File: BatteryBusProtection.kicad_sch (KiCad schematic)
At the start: 14 parts, among them Q10 SIRA99DP-T1-GE3, Q7 SIRA99DP-T1-GE3, Q8 SIRA99DP-T1-GE3, Q9 SIRA99DP-T1-GE3, U3 LTC4412xS6, U4 LTC4412xS6

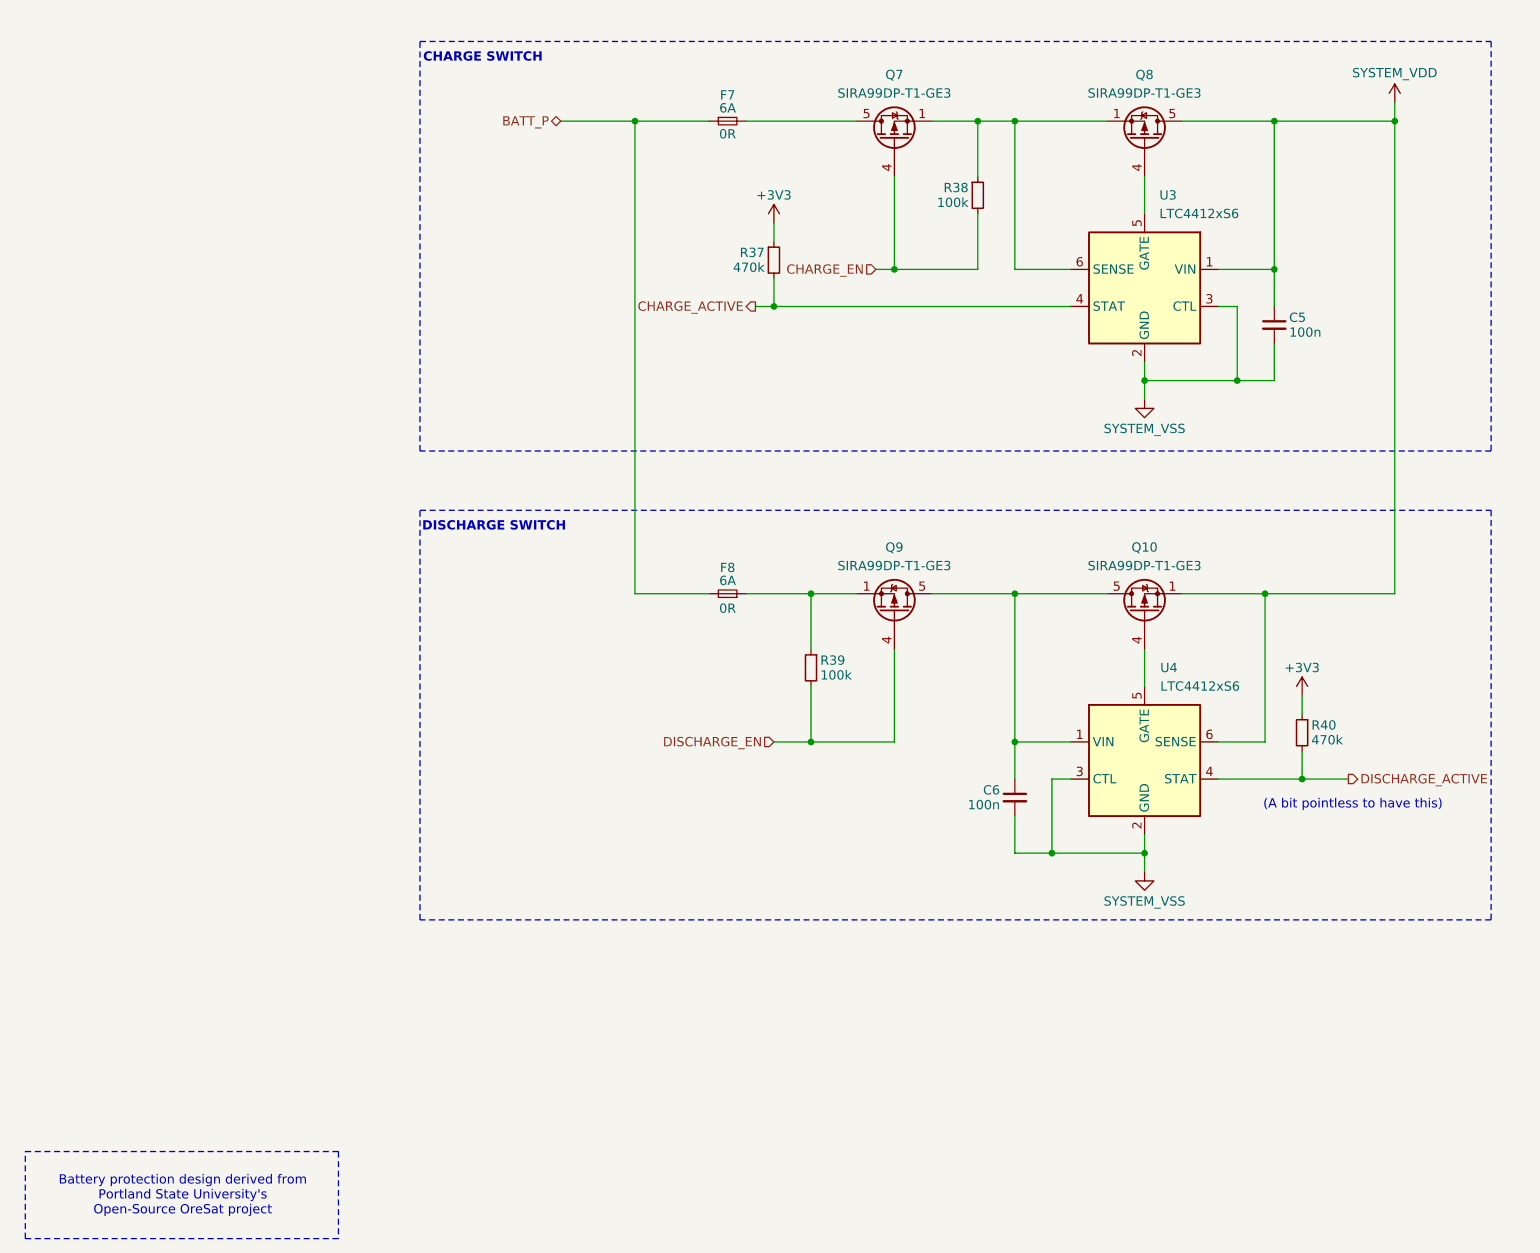
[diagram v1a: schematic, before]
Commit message: v3.2 Updates
Added 0ohm bypass. Opto-isolated heater enables
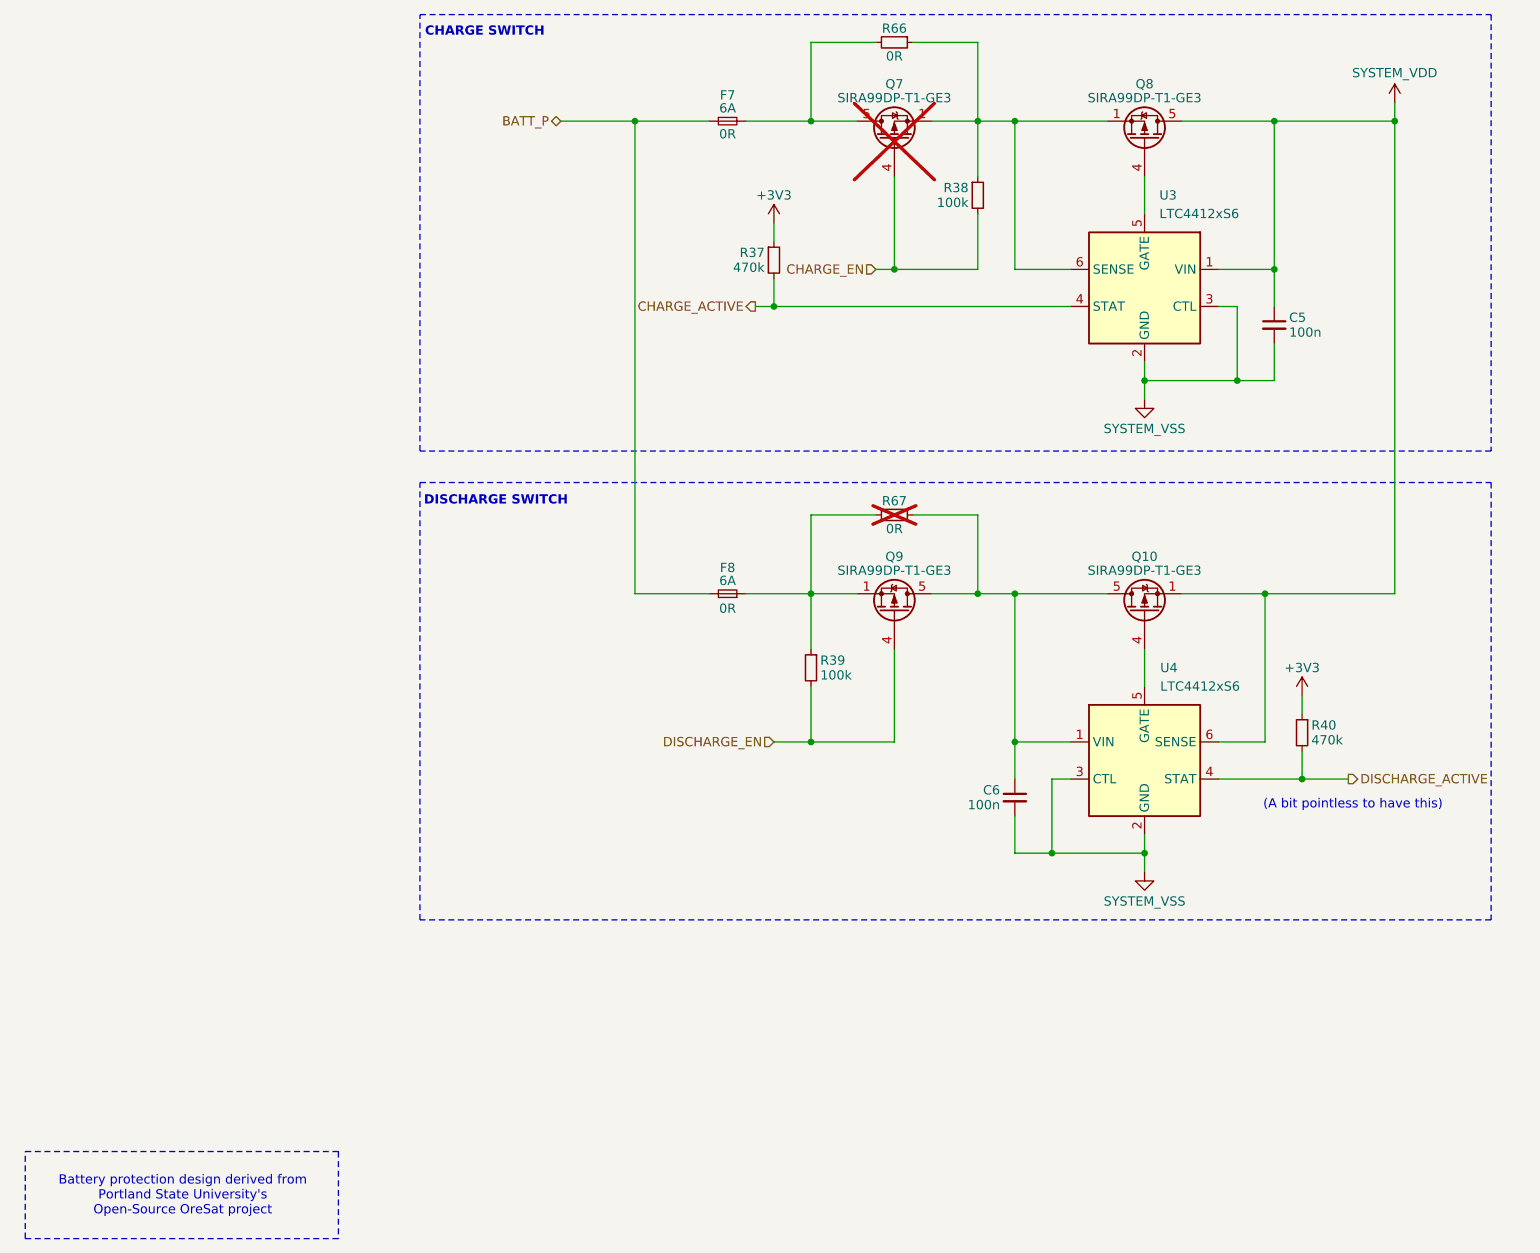
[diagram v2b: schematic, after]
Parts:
- added R66, R67: 0R, Resistor_SMD:R_1206_3216Metric, symbol Device:R_Small
- Q7: now not fitted; now left out of the parts list
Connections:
- net at F8.1, Q9.1 (S), Q9.2 (S)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: now also R67.2
- net at Q7.1 (S), Q7.2 (S), Q7.3 (S)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: now also R66.1
- net at F7.2, Q7.5 (D): now also R66.2
- net at C6.1, Q10.5 (D), Q9.5 (D)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: now also R67.1
